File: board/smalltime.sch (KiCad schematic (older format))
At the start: 46 parts, among them IC1 STM32F030K6T6, IC2 DS3231MZ, IC3 ADP3338, J1 MICROUSB, P1 SWD, P2 SWD_TC, Q1 TEPT4400, Q2 Q_NMOS_GDS, Q3 Q_NMOS_GDS, Q4 Q_NMOS_GDS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

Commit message: Nominally finished routing
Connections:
- net DIG2: now also IC1.6 (PA0); no longer IC1.30 (PB7)
- net DIG3: now also IC1.2 (PF0)
- net DIG4: now also IC1.3 (PF1)
- net DIG5: now also IC1.11 (PA5)
- net DIG6: now also IC1.20 (PA10)
- net DIG7: now also IC1.8 (PA2)
- net DIG8: now also IC1.7 (PA1)
- net I2C_SCL: now also IC1.29 (PB6)
- net I2C_SDA: now also IC1.30 (PB7)
- net LIGHT_EN: now also IC1.9 (PA3)
- net LIGHT_SENSE: now also IC1.10 (PA4)
- net SW_INC: now also IC1.18 (PA8)
- net SW_SET: now also IC1.19 (PA9)
- net at IC1.12 (PA6): now also R8.2
- net at IC1.13 (PA7): now also R7.2
- net at IC1.14 (PB0): now also R6.2
- net at IC1.15 (PB1): now also R11.2
- net at IC1.22 (PA12): now also R5.2
- net at IC1.26 (PB3): now also R4.2; no longer R5.2
- net at IC1.27 (PB4): now also R9.2; no longer R4.2
- net at IC1.28 (PB5): now also R10.2; no longer R9.2
- no-connect marks 10 -> 11
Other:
- moved on the sheet: IC1, P1, P2, R10, R11, R4, R5, R6, R7, R8, R9

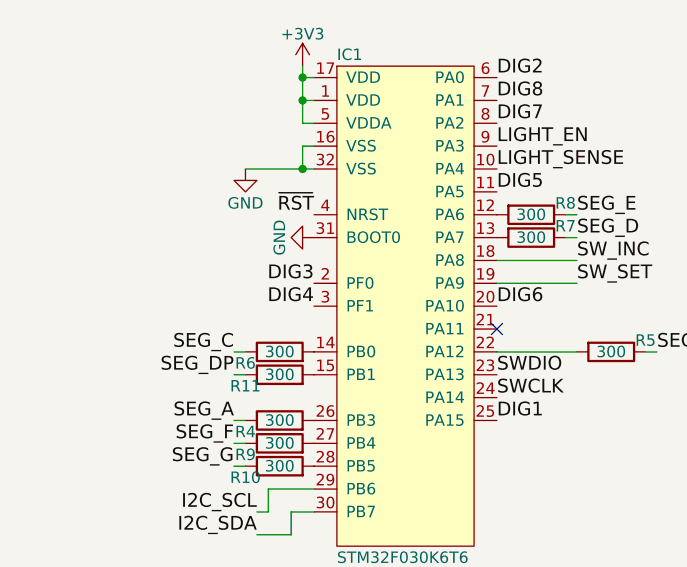
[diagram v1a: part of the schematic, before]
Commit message: minor routing improvements
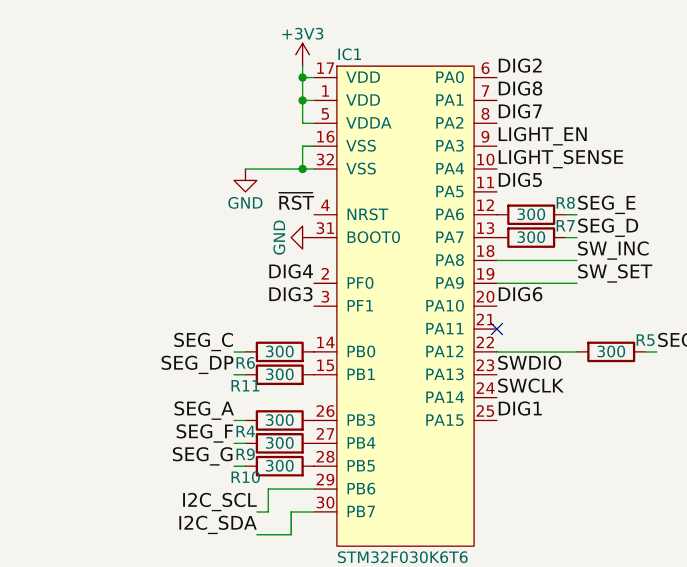
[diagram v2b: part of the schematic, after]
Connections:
- net DIG3: now also IC1.3 (PF1); no longer IC1.2 (PF0)
- net DIG4: now also IC1.2 (PF0); no longer IC1.3 (PF1)
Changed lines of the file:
@@
 LIBS:ds3231mz
 LIBS:mcp1700
-LIBS:si5515cdc
 LIBS:pfet
 LIBS:tept
@@
 Text Label 2900 2250 0    60   ~ 0
 DIG2
+Text Label 2100 3250 2    60   ~ 0
+DIG3
 Text Label 2100 3150 2    60   ~ 0
-DIG3
-Text Label 2100 3250 2    60   ~ 0
 DIG4
 Text Label 2900 2750 0    60   ~ 0

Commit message: Schematic checking/finishing
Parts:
- removed Q2, Q3, Q4, Q5, Q6, Q7, Q8, Q9: Q_NMOS_GDS, agg:SOT-23, symbol Q_NMOS_GDS
- added Q2, Q3, Q4, Q5, Q6, Q7, Q8, Q9: Q_NMOS_GSD, agg:SOT-23, symbol Q_NMOS_GSD
- R10, R11, R4, R5, R6, R7, R8, R9: value 300 -> 160; Farnell 2447331 -> 2447260
- U1, U2, U3, U4, U5, U6, U7, U8: Farnell 2627652 -> 2627651
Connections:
- net DIG1: now also Q2.1 (G)
- net DIG2: now also Q3.1 (G)
- net DIG3: now also Q4.1 (G)
- net DIG4: now also Q5.1 (G)
- net DIG5: now also Q6.1 (G)
- net DIG6: now also Q7.1 (G)
- net DIG7: now also Q8.1 (G)
- net DIG8: now also Q9.1 (G)
- net GND: now also Q2.2 (S), Q3.2 (S), Q4.2 (S), Q5.2 (S), Q6.2 (S), Q7.2 (S), Q8.2 (S), Q9.2 (S)
- net at U2.3 (CATH), U2.8 (CATH): now also Q3.3 (D)
- net at U3.3 (CATH), U3.8 (CATH): now also Q4.3 (D)
- net at U4.3 (CATH), U4.8 (CATH): now also Q5.3 (D)
- net at U5.3 (CATH), U5.8 (CATH): now also Q6.3 (D)
- net at U6.3 (CATH), U6.8 (CATH): now also Q7.3 (D)
- net at U7.3 (CATH), U7.8 (CATH): now also Q8.3 (D)
- net at U8.3 (CATH), U8.8 (CATH): now also Q9.3 (D)
- net at U1.3 (CATH), U1.8 (CATH): now also Q2.3 (D)

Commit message: Finishing touches and checking, silk
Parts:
- added TP1: SDA, smalltime:testpoint, symbol TEST
- added TP2: SCL, smalltime:testpoint, symbol TEST
- added TP3: GND, smalltime:testpoint, symbol TEST
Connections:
- net GND: now also TP3.1
- net I2C_SCL: now also TP2.1
- net I2C_SDA: now also TP1.1
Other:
- moved on the sheet: Q1, R3
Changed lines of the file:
@@
 	0    1    1    0
 $EndComp
-Text Label 3450 6300 2    60   ~ 0
+Text Label 2750 6300 2    60   ~ 0
 I2C_SDA
-Text Label 3450 6400 2    60   ~ 0
+Text Label 2750 6400 2    60   ~ 0
 I2C_SCL
 NoConn ~ 5550 5700
@@
 L TEPT Q1
 U 1 1 59739A13
-P 2150 6200
-F 0 "Q1" H 2300 5975 60  0000 C CNN
-F 1 "TEPT4400" H 2450 6450 60  0000 C CNN
-F 2 "LEDs:LED_D3.0mm" H 2025 6600 60  0001 C CNN
-F 3 "" H 2025 6600 60  0000 C CNN
-F 4 "SC12389" H 2150 6200 60  0001 C CNN "Farnell"
-	1    2150 6200
-	1    0    0    -1
-$EndComp
-Text Label 2200 5850 2    60   ~ 0
+P 1150 5200
+F 0 "Q1" H 1300 4975 60  0000 C CNN
+F 1 "TEPT4400" H 1450 5450 60  0000 C CNN
+F 2 "LEDs:LED_D3.0mm" H 1025 5600 60  0001 C CNN
+F 3 "" H 1025 5600 60  0000 C CNN
+F 4 "SC12389" H 1150 5200 60  0001 C CNN "Farnell"
+	1    1150 5200
+	1    0    0    -1
+$EndComp
+Text Label 1200 4850 2    60   ~ 0
 LIGHT_EN
 $Comp
 L R R3
 U 1 1 5973A47D
-P 2200 6800
-F 0 "R3" V 2280 6800 50  0000 C CNN
-F 1 "100k" V 2200 6800 50  0000 C CNN
-F 2 "agg:0603" V 2130 6800 50  0001 C CNN
-F 3 "" H 2200 6800 50  0001 C CNN
-F 4 "2447226" H 2200 6800 60  0001 C CNN "Farnell"
-	1    2200 6800
+P 1200 5800
+F 0 "R3" V 1280 5800 50  0000 C CNN
+F 1 "100k" V 1200 5800 50  0000 C CNN
+F 2 "agg:0603" V 1130 5800 50  0001 C CNN
+F 3 "" H 1200 5800 50  0001 C CNN
+F 4 "2447226" H 1200 5800 60  0001 C CNN "Farnell"
+	1    1200 5800
 	1    0    0    -1
 $EndComp
@@
 L GND #PWR028
 U 1 1 5973A502
-P 2200 6950
-F 0 "#PWR028" H 2200 6700 50  0001 C CNN
-F 1 "GND" H 2200 6800 50  0000 C CNN
-F 2 "" H 2200 6950 50  0001 C CNN
-F 3 "" H 2200 6950 50  0001 C CNN
-	1    2200 6950
-	1    0    0    -1
-$EndComp
-Wire Wire Line
-	2200 6550 2200 6650
-Wire Wire Line
-	2200 6600 2300 6600
-Connection ~ 2200 6600
-Text Label 2300 6600 0    60   ~ 0
+P 1200 5950
+F 0 "#PWR028" H 1200 5700 50  0001 C CNN
+F 1 "GND" H 1200 5800 50  0000 C CNN
+F 2 "" H 1200 5950 50  0001 C CNN
+F 3 "" H 1200 5950 50  0001 C CNN
+	1    1200 5950
+	1    0    0    -1
+$EndComp
+Wire Wire Line
+	1200 5550 1200 5650
+Wire Wire Line
+	1200 5600 1300 5600
+Connection ~ 1200 5600
+Text Label 1300 5600 0    60   ~ 0
 LIGHT_SENSE
 Text Label 2900 2550 0    60   ~ 0
@@
 	3950 5750 4300 5750
 Wire Wire Line
-	3450 6300 4150 6300
+	2750 6300 4150 6300
 Wire Wire Line
 	4150 6300 4150 6100
@@
 	4250 6200 4250 6400
 Wire Wire Line
-	4250 6400 3450 6400
+	4250 6400 2750 6400
 Wire Wire Line
 	3550 6250 3550 6300
@@
 	-1   0    0    -1
 $EndComp
+$Comp
+L TEST TP1
+U 1 1 5980F23A
+P 2850 6100
+F 0 "TP1" H 2928 6240 50  0000 L CNN
+F 1 "SDA" H 2928 6149 50  0000 L CNN
+F 2 "smalltime:testpoint" H 2850 6100 50  0001 C CNN
+F 3 "" H 2850 6100 50  0001 C CNN
+	1    2850 6100
+	1    0    0    -1
+$EndComp
+$Comp
+L TEST TP2
+U 1 1 5980FCC3
+P 3150 6100
+F 0 "TP2" H 3228 6240 50  0000 L CNN
+F 1 "SCL" H 3228 6149 50  0000 L CNN
+F 2 "smalltime:testpoint" H 3150 6100 50  0001 C CNN
+F 3 "" H 3150 6100 50  0001 C CNN
+	1    3150 6100
+	1    0    0    -1
+$EndComp
+Wire Wire Line
+	2850 6100 2850 6300
+Connection ~ 2850 6300
+Wire Wire Line
+	3150 6100 3150 6400
+Connection ~ 3150 6400
+$Comp
+L TEST TP3
+U 1 1 59810BF4
+P 2200 6100
+F 0 "TP3" H 2278 6240 50  0000 L CNN
+F 1 "GND" H 2278 6149 50  0000 L CNN
+F 2 "smalltime:testpoint" H 2200 6100 50  0001 C CNN
+F 3 "" H 2200 6100 50  0001 C CNN
+	1    2200 6100
+	1    0    0    -1
+$EndComp
+$Comp
+L GND #PWR?
+U 1 1 598110F8
+P 2200 6100
+F 0 "#PWR?" H 2200 5850 50  0001 C CNN
+F 1 "GND" H 2205 5927 50  0000 C CNN
+F 2 "" H 2200 6100 50  0001 C CNN
+F 3 "" H 2200 6100 50  0001 C CNN
+	1    2200 6100
+	1    0    0    -1
+$EndComp
 $EndSCHEMATC

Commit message: Add 1kR order#, add BOM
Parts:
- R1, R2: Farnell (none) -> 2447272
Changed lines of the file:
@@
 F 2 "agg:0603" V 3630 6100 50  0001 C CNN
 F 3 "" H 3700 6100 50  0001 C CNN
+F 4 "2447272" H 3700 6100 60  0001 C CNN "Farnell"
 	1    3700 6100
 	1    0    0    -1
@@
 F 2 "agg:0603" V 3480 6100 50  0001 C CNN
 F 3 "" H 3550 6100 50  0001 C CNN
+F 4 "2447272" H 3550 6100 60  0001 C CNN "Farnell"
 	1    3550 6100
 	1    0    0    -1
@@
 $EndComp
 $Comp
-L GND #PWR?
+L GND #PWR041
 U 1 1 598110F8
 P 2200 6100
-F 0 "#PWR?" H 2200 5850 50  0001 C CNN
+F 0 "#PWR041" H 2200 5850 50  0001 C CNN
 F 1 "GND" H 2205 5927 50  0000 C CNN
 F 2 "" H 2200 6100 50  0001 C CNN

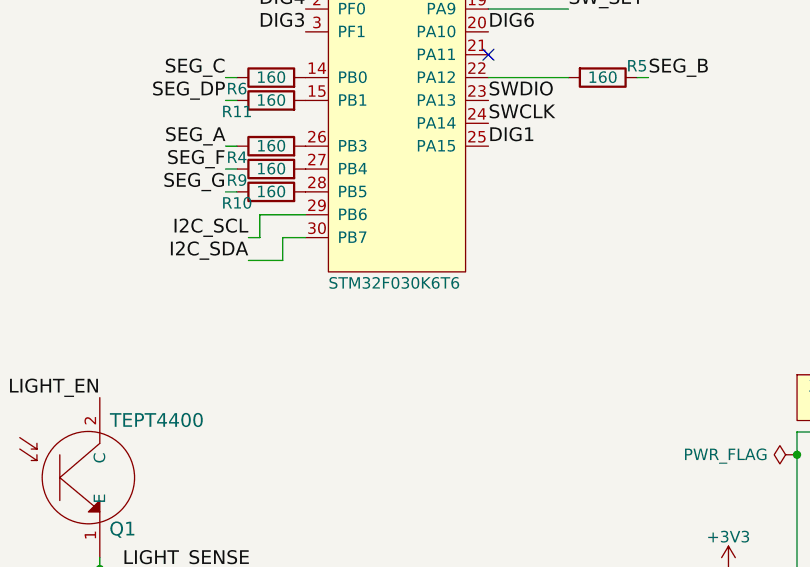
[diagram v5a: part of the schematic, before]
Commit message: Replace STM32F030K6 with STM32F051K6 for more RAM
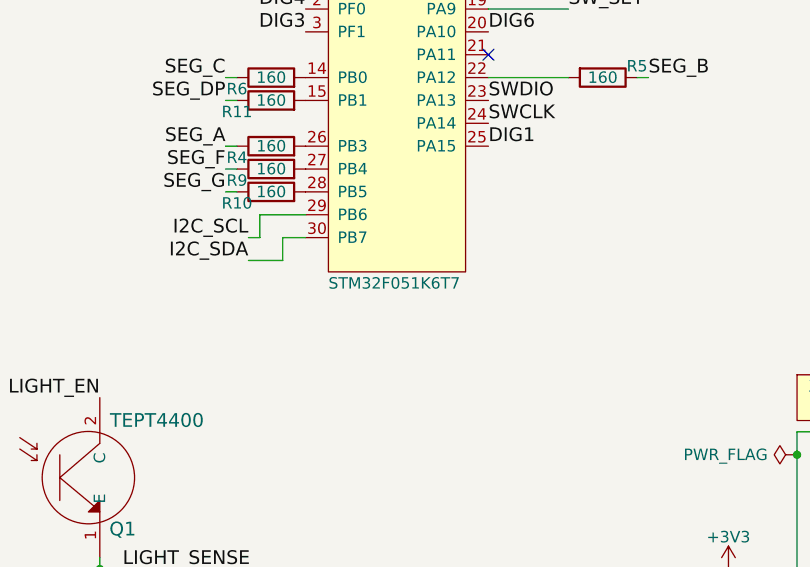
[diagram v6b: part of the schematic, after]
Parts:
- IC1: value STM32F030K6T6 -> STM32F051K6T7; Farnell 2432085 -> 2432090
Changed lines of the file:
@@
 LIBS:ds3231mz
 LIBS:mcp1700
-LIBS:si5515cdc
 LIBS:pfet
 LIBS:tept
@@
 P 2500 3250
 F 0 "IC1" H 2200 4350 50  0000 L CNN
-F 1 "STM32F030K6T6" H 2200 2150 50  0000 L CNN
+F 1 "STM32F051K6T7" H 2200 2150 50  0000 L CNN
 F 2 "agg:LQFP-32" H 2200 2050 50  0001 L CNN
-F 3 "http://www.st.com/web/en/resource/technical/document/datasheet/DM00088500.pdf" H 2200 1950 50  0001 L CNN
-F 4 "2432085" H 2200 1850 50  0001 L CNN "Farnell"
+F 3 "http://www.farnell.com/datasheets/2307889.pdf" H 2200 1950 50  0001 L CNN
+F 4 "2432090" H 2200 1850 50  0001 L CNN "Farnell"
 	1    2500 3250
 	1    0    0    -1

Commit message: Change ADP3338 to 3v3 part
BOM accidentally had 5V output ADP3338: change farnell part to 3v3 one.
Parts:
- IC3: Farnell 1651284 -> 1651283
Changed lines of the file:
@@
 LIBS:ds3231mz
 LIBS:mcp1700
+LIBS:si5515cdc
 LIBS:pfet
 LIBS:tept
@@
 F 2 "agg-unchecked:SOT223" H 5500 6550 50  0001 L CNN
 F 3 "http://www.farnell.com/datasheets/2254554.pdf" H 5700 6850 50  0001 C CNN
-F 4 "1651284" H 5500 6450 50  0001 L CNN "Farnell"
+F 4 "1651283" H 5500 6450 50  0001 L CNN "Farnell"
 	1    5700 6850
 	1    0    0    -1
